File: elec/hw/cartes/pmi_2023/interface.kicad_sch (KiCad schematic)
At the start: 41 parts, among them SW3 MSS12C02LS-BB2.0, SW4 TM-4175-B-A, SW5 HAD-04HWAG-2, U11 TCA6408ARGTR, U18 RPI-0352E, U24 SN74LVC2G17DBV, U25 SN74LVC2G17DBV

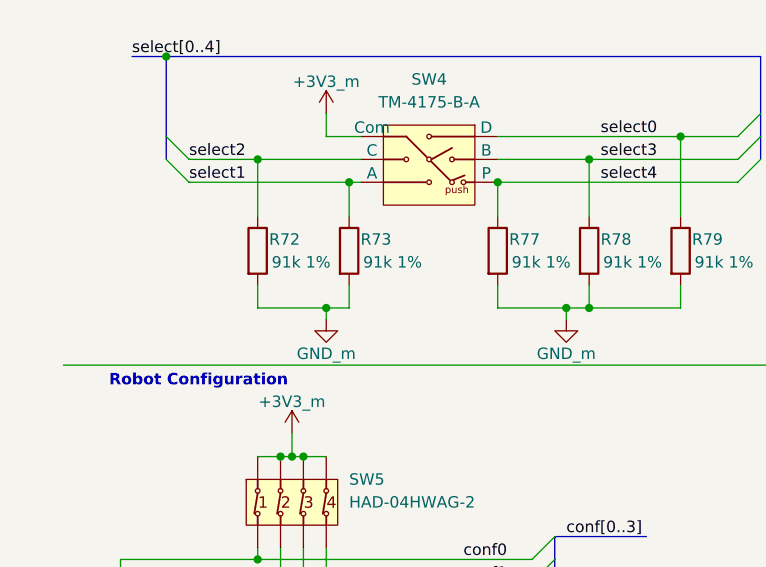
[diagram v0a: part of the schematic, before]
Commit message: review number 3 taken into account
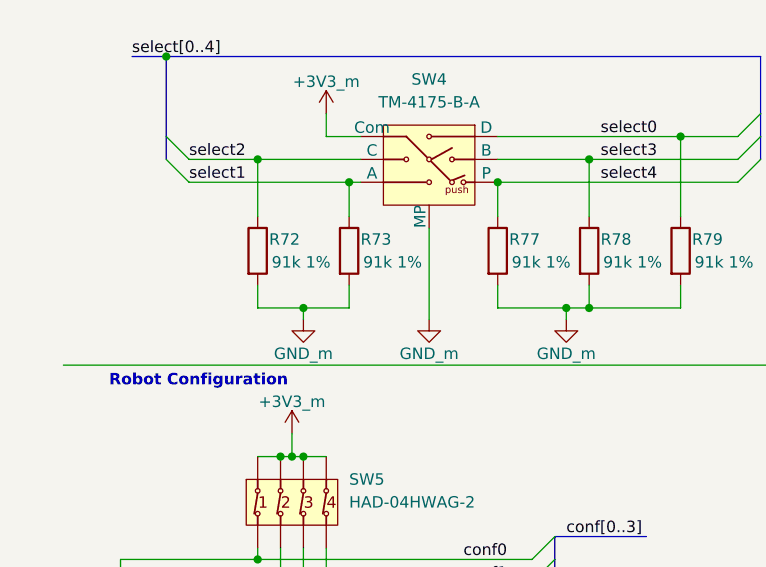
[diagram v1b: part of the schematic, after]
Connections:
- net GND_m: now also SW4.MP
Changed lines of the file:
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@@
 	)
 	(junction
-		(at 43.18 144.78)
+		(at 176.53 151.13)
 		(diameter 0)
 		(color 0 0 0 0)
 	)
 	(junction
-		(at 176.53 151.13)
+		(at 38.1 175.26)
 		(diameter 0)
 		(color 0 0 0 0)
 	)
 	(junction
-		(at 38.1 175.26)
+		(at 111.76 139.7)
 		(diameter 0)
 		(color 0 0 0 0)
 	)
 	(junction
-		(at 111.76 139.7)
+		(at 40.64 144.78)
 		(diameter 0)
 		(color 0 0 0 0)
@@
 	(wire
 		(pts
+			(xy 40.64 144.78) (xy 45.72 144.78)
+		)
+		(stroke
+			(width 0)
+			(type default)
+		)
+	)
+	(wire
+		(pts
 			(xy 40.64 171.45) (xy 40.64 177.8)
 		)
@@
 	(wire
 		(pts
-			(xy 43.18 146.05) (xy 43.18 144.78)
+			(xy 40.64 146.05) (xy 40.64 144.78)
 		)
 		(stroke
@@
 	(wire
 		(pts
-			(xy 35.56 144.78) (xy 43.18 144.78)
+			(xy 35.56 144.78) (xy 40.64 144.78)
 		)
 		(stroke
@@
 	(wire
 		(pts
-			(xy 43.18 144.78) (xy 45.72 144.78)
-		)
-		(stroke
-			(width 0)
-			(type default)
-		)
-	)
-	(wire
-		(pts
 			(xy 163.83 175.26) (xy 171.45 175.26)
 		)
@@
 	(wire
 		(pts
+			(xy 54.61 135.89) (xy 54.61 146.05)
+		)
+		(stroke
+			(width 0)
+			(type default)
+		)
+	)
+	(wire
+		(pts
 			(xy 53.34 30.48) (xy 53.34 29.21)
 		)
@@
 	)
 	(symbol
+		(lib_id "pmi_2023_specific:GND_m")
+		(at 54.61 146.05 0)
+		(unit 1)
+		(exclude_from_sim no)
+		(in_bom yes)
+		(on_board yes)
+		(dnp no)
+		(property "Reference" "#PWR0135"
+			(at 54.61 152.4 0)
+			(effects
+				(font
+					(size 1.27 1.27)
+				)
+				(hide yes)
+			)
+		)
+		(property "Value" "GND_m"
+			(at 54.61 149.86 0)
+			(effects
+				(font
+					(size 1.27 1.27)
+				)
+			)
+		)
+		(property "Footprint" ""
+			(at 54.61 146.05 0)
+			(effects
+				(font
+					(size 1.27 1.27)
+				)
+				(hide yes)
+			)
+		)
+		(property "Datasheet" ""
+			(at 54.61 146.05 0)
+			(effects
+				(font
+					(size 1.27 1.27)
+				)
+				(hide yes)
+			)
+		)
+		(property "Description" "Power symbol creates a global label with name \"GND\" , ground"
+			(at 54.61 146.05 0)
+			(effects
+				(font
+					(size 1.27 1.27)
+				)
+				(hide yes)
+			)
+		)
+		(pin "1"
+		)
+		(instances
+			(project "pmi_2023"
+				(path "/334a657f-c66c-4260-9567-14f1c99913d7/9da1923e-9bb0-4408-8ee2-582c85dcd497/70ec626c-1f87-41a0-95c0-5e3c50204455"
+					(reference "#PWR0135")
+					(unit 1)
+				)
+			)
+		)
+	)
+	(symbol
 		(lib_id "cocotter_resistors:R_1k_0603_1%")
 		(at 153.67 168.91 0)
@@
 		(pin "1"
 		)
+		(pin "MP"
+		)
 		(instances
 			(project "pmi_2023"
@@
 	(symbol
 		(lib_id "pmi_2023_specific:GND_m")
-		(at 43.18 146.05 0)
+		(at 40.64 146.05 0)
 		(unit 1)
 		(exclude_from_sim no)
@@
 		(dnp no)
 		(property "Reference" "#PWR017"
-			(at 43.18 152.4 0)
+			(at 40.64 152.4 0)
 			(effects
 				(font
@@
 		)
 		(property "Value" "GND_m"
-			(at 43.18 149.86 0)
+			(at 40.64 149.86 0)
 			(effects
 				(font
@@
 		)
 		(property "Footprint" ""
-			(at 43.18 146.05 0)
+			(at 40.64 146.05 0)
 			(effects
 				(font
@@
 		)
 		(property "Datasheet" ""
-			(at 43.18 146.05 0)
+			(at 40.64 146.05 0)
 			(effects
 				(font
@@
 		)
 		(property "Description" "Power symbol creates a global label with name \"GND\" , ground"
-			(at 43.18 146.05 0)
+			(at 40.64 146.05 0)
 			(effects
 				(font

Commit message: pmi board V2, ready for review
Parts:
- removed R80, R81: 1k 1%, cocotter_resistor:r0603_reflow, symbol cocotter_resistors:R_1k_0603_1%

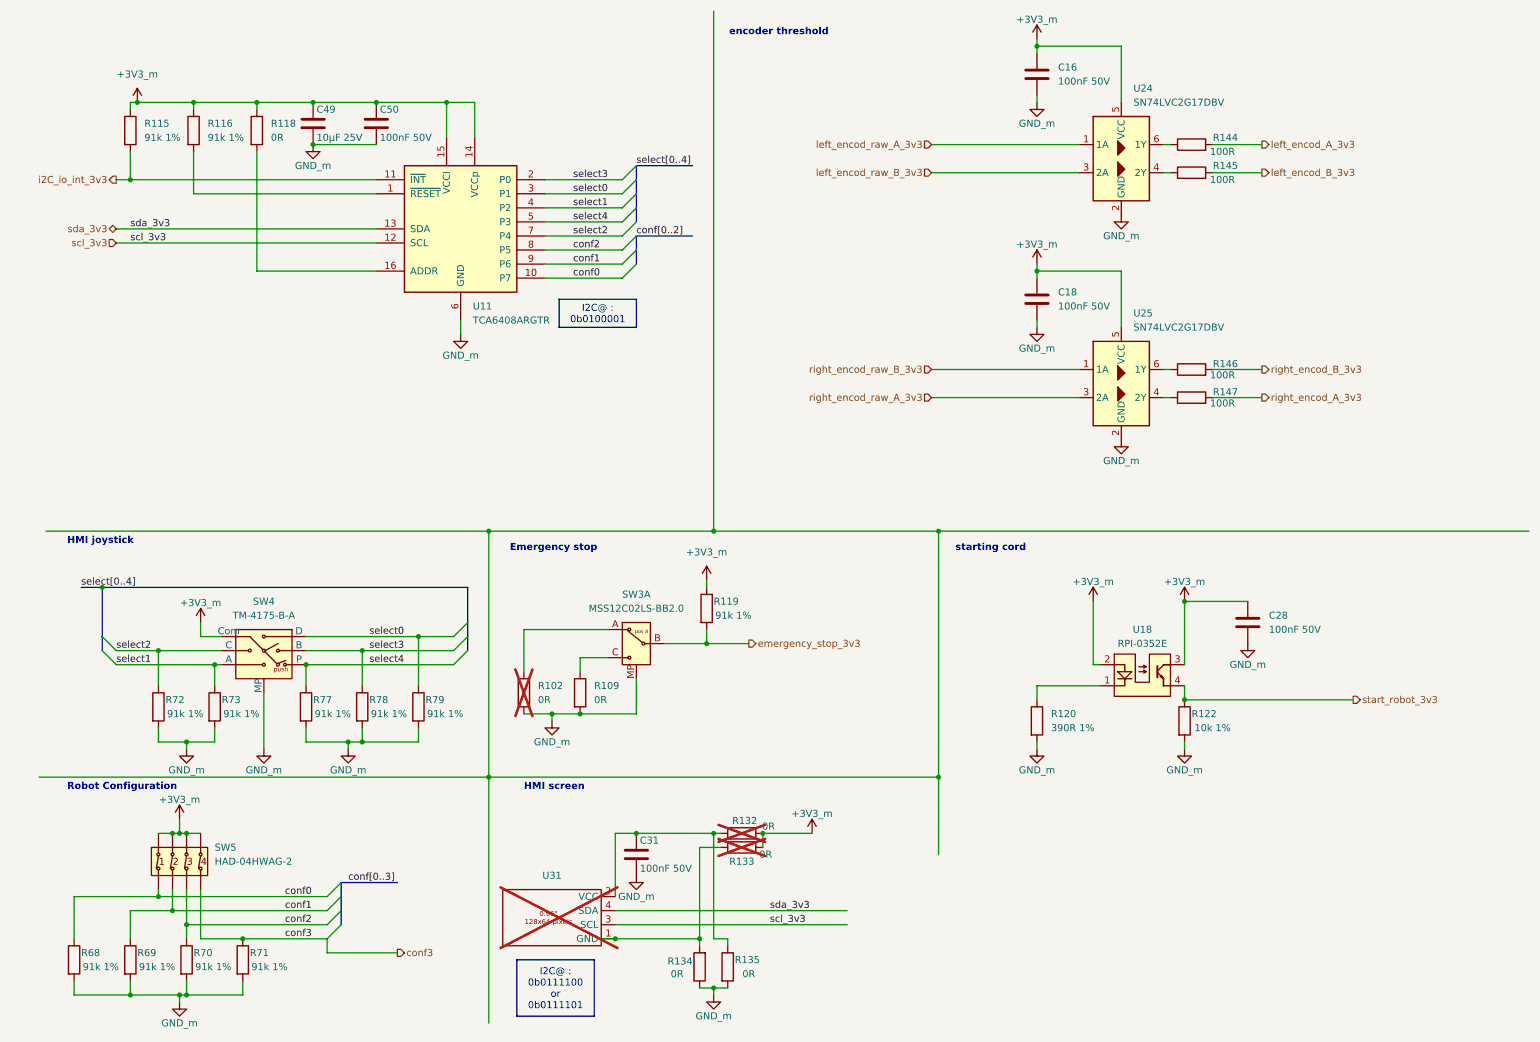
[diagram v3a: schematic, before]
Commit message: pmi: beginning of transition toward 0402 resistors and capacitors, battery gauge added
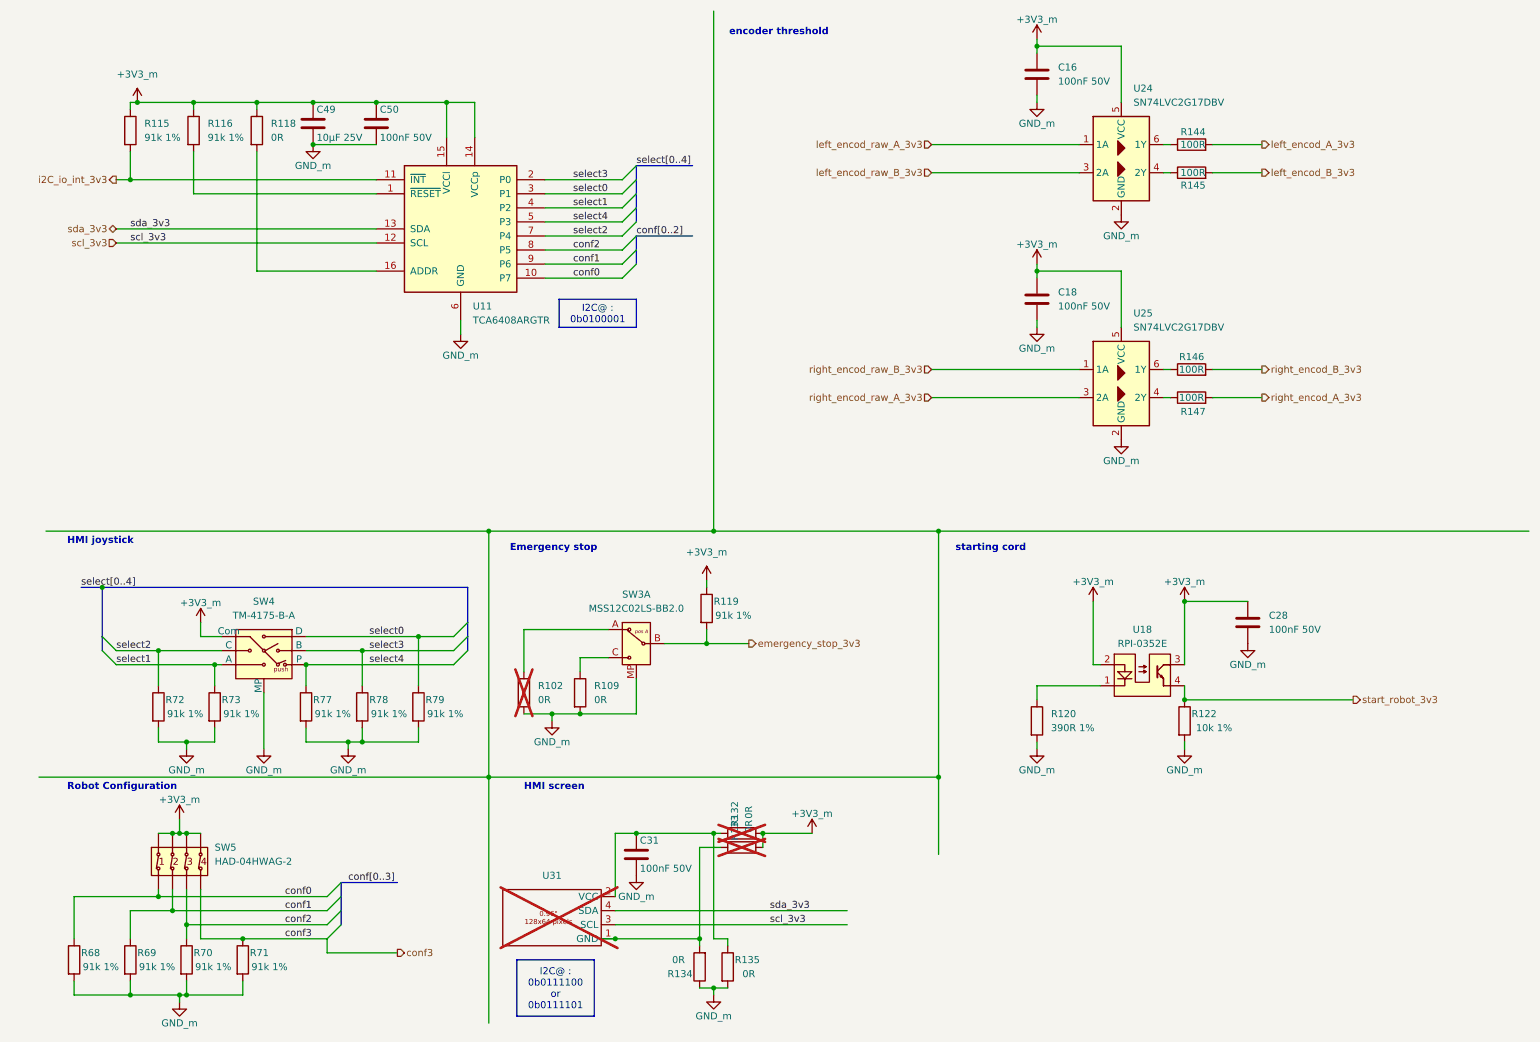
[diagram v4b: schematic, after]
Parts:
- C16, C18, C28, C31, C50: footprint cocotter_capacitors:C_0603_1608Metric -> cocotter_capacitors:C_0402_1005Metric; symbol cocotter_capacitors:C_100nF_50V_0603 -> cocotter_capacitors:C_100nF_50V_0402; JLCPCB Part # C14663 -> C85858; Specification 100nF 50V X7R 0603 -> 100nF 50V X7R 0402
- R102, R109, R118, R132, R133, R134, R135: footprint cocotter_resistor:r0603_reflow -> cocotter_resistor:r0402_reflow; symbol cocotter_resistors:R_0R_0603 -> cocotter_resistors:R_0R_0402; JLCPCB Part # C431718 -> C; Specification 0R 0603 20mOhms max 100mW -> 0R 0603
- R122: footprint cocotter_resistor:r0603_reflow -> cocotter_resistor:r0402_reflow; symbol cocotter_resistors:R_10k_0603_1% -> cocotter_resistors:R_10k_0402_1%; JLCPCB Part # C25804 -> C; Specification 10k 0603 1% 100mW -> 10k 0402 1% 100mW
- R144, R145, R146, R147: footprint cocotter_resistor:r0603_reflow -> cocotter_resistor:r0402_reflow; symbol cocotter_resistors:R_100R_0603_1% -> cocotter_resistors:R_100R_0402_1%; JLCPCB Part # C22775 -> C25076; Specification 100R 0603 1% 100mW -> 100R 0402 1% 62.5mW

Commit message: pmi2023 updated
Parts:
- added J10: 533980371, cocotter_connectors:533980371, symbol cocotter_connectors:533980371
- added J6: 533980571, cocotter_connectors:533980571, symbol cocotter_connectors:533980571
- added R84: 91k 1%, cocotter_resistor:r0603_reflow, symbol cocotter_resistors:R_91k_0603_1%
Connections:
- net +3V3_m: now also J6.5
- net GND_m: now also J10.1, J6.1, R84.2
- net scl_3v3: now also J6.2
- net sda_3v3: now also J6.3
- new net dig_servo_cmd_3v3: J6.4, R84.1
- new net scl_tof_3v3: J10.2
- new net sda_tof_3v3: J10.3
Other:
- moved on the sheet: C49, C50, R115, R116, R118, R120, U11

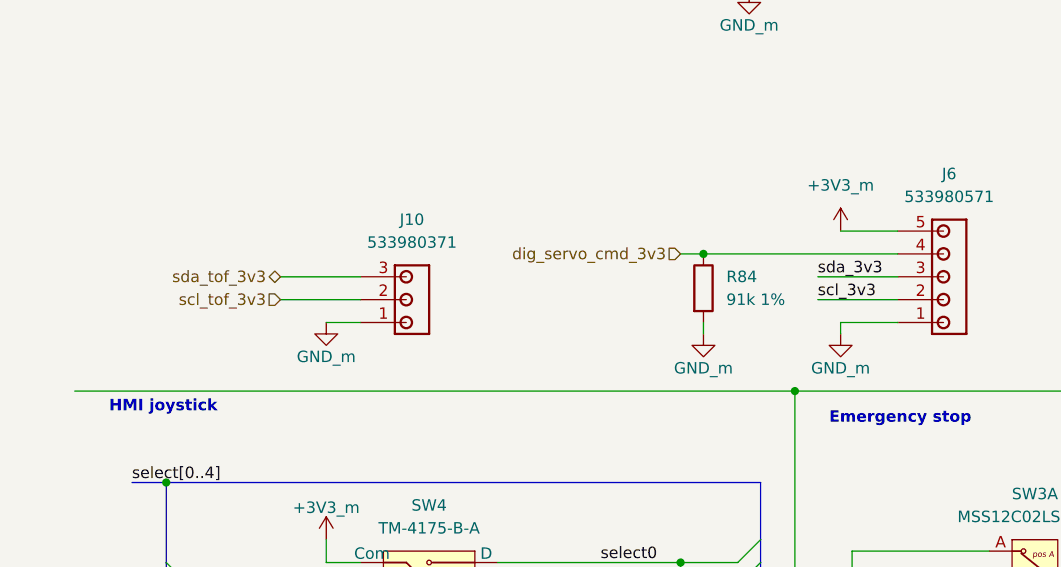
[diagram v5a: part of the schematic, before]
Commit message: pmi2023 : routing updated
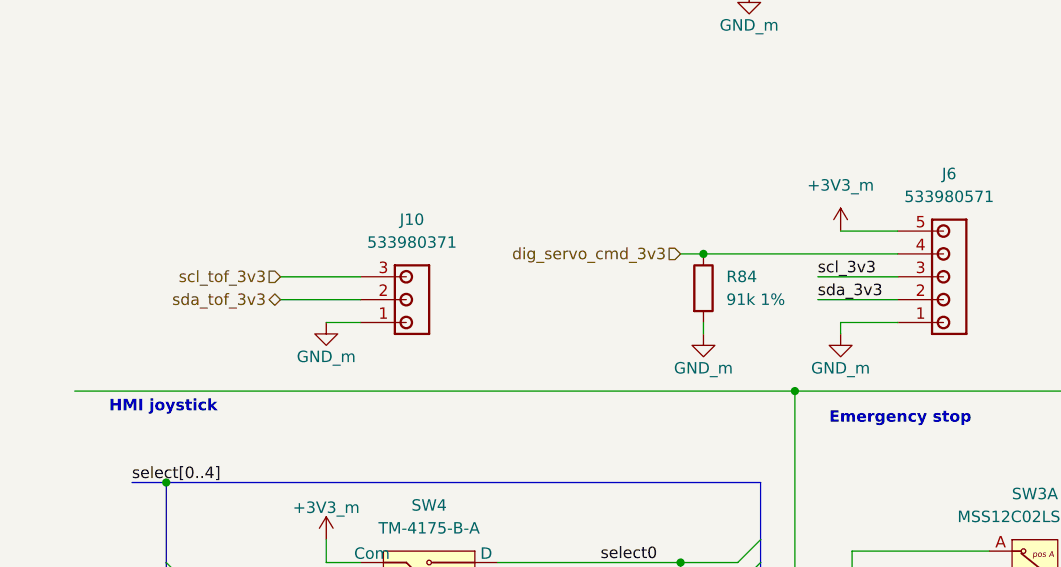
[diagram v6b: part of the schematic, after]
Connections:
- net scl_3v3: now also J6.3; no longer J6.2
- net scl_tof_3v3: now also J10.3; no longer J10.2
- net sda_3v3: now also J6.2; no longer J6.3
- net sda_tof_3v3: now also J10.2; no longer J10.3
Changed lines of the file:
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@@
 	)
 	(label "scl_3v3"
-		(at 97.79 96.52 0)
+		(at 97.79 93.98 0)
 		(effects
 			(font
@@
 	)
 	(label "sda_3v3"
-		(at 97.79 93.98 0)
+		(at 97.79 96.52 0)
 		(effects
 			(font
@@
 	(hierarchical_label "sda_tof_3v3"
 		(shape bidirectional)
-		(at 38.1 93.98 180)
+		(at 38.1 96.52 180)
 		(effects
 			(font
@@
 	(hierarchical_label "scl_tof_3v3"
 		(shape input)
-		(at 38.1 96.52 180)
-		(effects
-			(font
+		(at 38.1 93.98 180)
+		(effects
+			(font

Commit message: pmi2023 : corrections after review, digital servo added, battery connector added
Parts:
- R115, R116, R119, R68, R69, R70, R71, R72, R73, R77, R78, R79, R84: footprint cocotter_resistor:r0603_reflow -> cocotter_resistor:r0402_reflow; symbol cocotter_resistors:R_91k_0603_1% -> cocotter_resistors:R_91k_0402_1%; JLCPCB Part # C23265 -> C327323; Specification 91k 0603 1% 100mW -> 91k 0402 1% 100mW
